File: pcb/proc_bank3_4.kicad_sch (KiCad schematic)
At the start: 2 parts, among them U1 XC6SLX9-TQG144

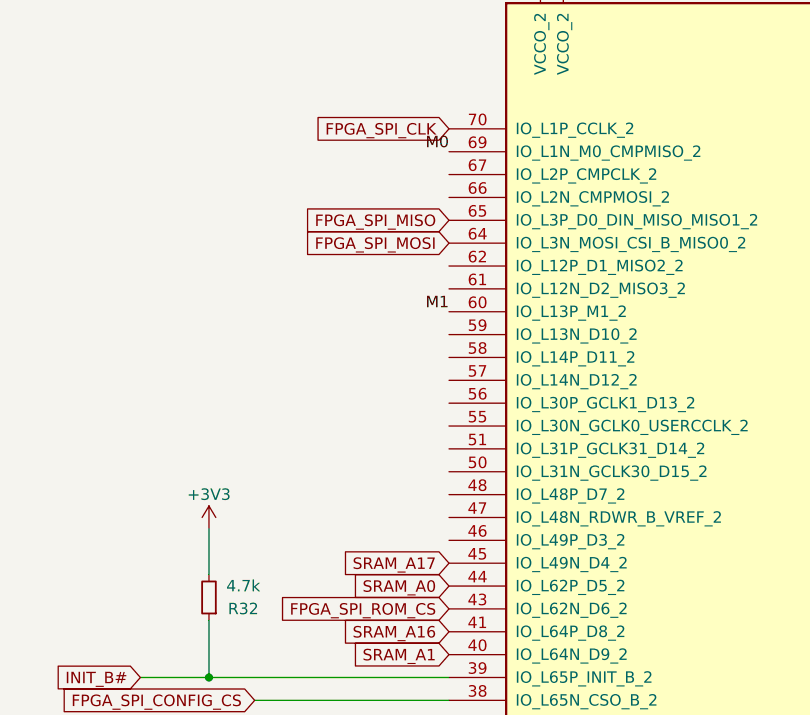
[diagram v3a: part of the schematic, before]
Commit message: edit the connector pinout
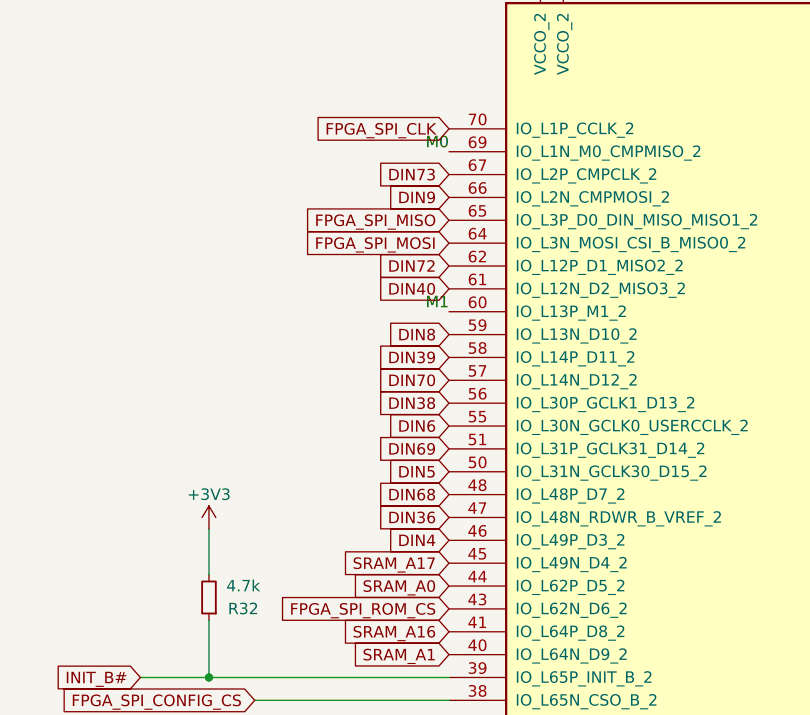
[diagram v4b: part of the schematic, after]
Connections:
- net DIN4: now reaches U1.46 (IO_L49P_D3_2)
- net DIN36: now reaches U1.47 (IO_L48N_RDWR_B_VREF_2)
- net DIN68: now reaches U1.48 (IO_L48P_D7_2)
- net DIN5: now reaches U1.50 (IO_L31N_GCLK30_D15_2)
- net DIN69: now reaches U1.51 (IO_L31P_GCLK31_D14_2)
- net DIN6: now reaches U1.55 (IO_L30N_GCLK0_USERCCLK_2)
- net DIN38: now reaches U1.56 (IO_L30P_GCLK1_D13_2)
- net DIN70: now reaches U1.57 (IO_L14N_D12_2)
- net DIN39: now reaches U1.58 (IO_L14P_D11_2)
- net DIN8: now reaches U1.59 (IO_L13N_D10_2)
- net DIN40: now reaches U1.61 (IO_L12N_D2_MISO3_2)
- net DIN72: now reaches U1.62 (IO_L12P_D1_MISO2_2)
- net DIN9: now reaches U1.66 (IO_L2N_CMPMOSI_2)
- net DIN73: now reaches U1.67 (IO_L2P_CMPCLK_2)
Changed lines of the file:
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@@
-(kicad_sch (version 20210621) (generator eeschema)
+(kicad_sch (version 20210406) (generator eeschema)
   (paper "User" 280.01 180.01)
   (junction (at 107.95 116.84) (diameter 0.9144) (color 0 0 0 0))
@@
     )
   )
+  (global_label "DIN73" (shape input) (at 134.62 60.96 180) (fields_autoplaced)
+    (effects (font (size 1.27 1.27)) (justify right))
+    (property "Intersheet References" "${INTERSHEET_REFS}" (id 0) (at 126.5826 60.8806 0)
+      (effects (font (size 1.27 1.27)) (justify right) hide)
+    )
+  )
+  (global_label "DIN9" (shape input) (at 134.62 63.5 180) (fields_autoplaced)
+    (effects (font (size 1.27 1.27)) (justify right))
+    (property "Intersheet References" "${INTERSHEET_REFS}" (id 0) (at 127.7921 63.4206 0)
+      (effects (font (size 1.27 1.27)) (justify right) hide)
+    )
+  )
   (global_label "FPGA_SPI_MISO" (shape input) (at 134.62 66.04 180) (fields_autoplaced)
     (effects (font (size 1.27 1.27)) (justify right))
@@
       (effects (font (size 1.27 1.27)) (justify right) hide)
     )
+  )
+  (global_label "DIN72" (shape input) (at 134.62 71.12 180) (fields_autoplaced)
+    (effects (font (size 1.27 1.27)) (justify right))
+    (property "Intersheet References" "${INTERSHEET_REFS}" (id 0) (at 126.5826 71.0406 0)
+      (effects (font (size 1.27 1.27)) (justify right) hide)
+    )
+  )
+  (global_label "DIN40" (shape input) (at 134.62 73.66 180) (fields_autoplaced)
+    (effects (font (size 1.27 1.27)) (justify right))
+    (property "Intersheet References" "${INTERSHEET_REFS}" (id 0) (at 126.5826 73.5806 0)
+      (effects (font (size 1.27 1.27)) (justify right) hide)
+    )
+  )
+  (global_label "DIN8" (shape input) (at 134.62 78.74 180) (fields_autoplaced)
+    (effects (font (size 1.27 1.27)) (justify right))
+    (property "Intersheet References" "${INTERSHEET_REFS}" (id 0) (at 127.7921 78.6606 0)
+      (effects (font (size 1.27 1.27)) (justify right) hide)
+    )
+  )
+  (global_label "DIN39" (shape input) (at 134.62 81.28 180) (fields_autoplaced)
+    (effects (font (size 1.27 1.27)) (justify right))
+    (property "Intersheet References" "${INTERSHEET_REFS}" (id 0) (at 126.5826 81.2006 0)
+      (effects (font (size 1.27 1.27)) (justify right) hide)
+    )
+  )
+  (global_label "DIN70" (shape input) (at 134.62 83.82 180) (fields_autoplaced)
+    (effects (font (size 1.27 1.27)) (justify right))
+    (property "Intersheet References" "${INTERSHEET_REFS}" (id 0) (at 126.5826 83.7406 0)
+      (effects (font (size 1.27 1.27)) (justify right) hide)
+    )
+  )
+  (global_label "DIN38" (shape input) (at 134.62 86.36 180) (fields_autoplaced)
+    (effects (font (size 1.27 1.27)) (justify right))
+    (property "Intersheet References" "${INTERSHEET_REFS}" (id 0) (at 126.5826 86.2806 0)
+      (effects (font (size 1.27 1.27)) (justify right) hide)
+    )
+  )
+  (global_label "DIN6" (shape input) (at 134.62 88.9 180) (fields_autoplaced)
+    (effects (font (size 1.27 1.27)) (justify right))
+    (property "Intersheet References" "${INTERSHEET_REFS}" (id 0) (at 127.7921 88.8206 0)
+      (effects (font (size 1.27 1.27)) (justify right) hide)
+    )
+  )
+  (global_label "DIN69" (shape input) (at 134.62 91.44 180) (fields_autoplaced)
+    (effects (font (size 1.27 1.27)) (justify right))
+    (property "Intersheet References" "${INTERSHEET_REFS}" (id 0) (at 126.5826 91.3606 0)
+      (effects (font (size 1.27 1.27)) (justify right) hide)
+    )
+  )
+  (global_label "DIN5" (shape input) (at 134.62 93.98 180) (fields_autoplaced)
+    (effects (font (size 1.27 1.27)) (justify right))
+    (property "Intersheet References" "${INTERSHEET_REFS}" (id 0) (at 127.7921 93.9006 0)
+      (effects (font (size 1.27 1.27)) (justify right) hide)
+    )
+  )
+  (global_label "DIN68" (shape input) (at 134.62 96.52 180) (fields_autoplaced)
+    (effects (font (size 1.27 1.27)) (justify right))
+    (property "Intersheet References" "${INTERSHEET_REFS}" (id 0) (at 126.5826 96.4406 0)
+      (effects (font (size 1.27 1.27)) (justify right) hide)
+    )
+  )
+  (global_label "DIN36" (shape input) (at 134.62 99.06 180) (fields_autoplaced)
+    (effects (font (size 1.27 1.27)) (justify right))
+    (property "Intersheet References" "${INTERSHEET_REFS}" (id 0) (at 126.5826 98.9806 0)
+      (effects (font (size 1.27 1.27)) (justify right) hide)
+    )
+  )
+  (global_label "DIN4" (shape input) (at 134.62 101.6 180) (fields_autoplaced)
+    (effects (font (size 1.27 1.27)) (justify right))
+    (property "Intersheet References" "${INTERSHEET_REFS}" (id 0) (at 127.7921 101.5206 0)
+      (effects (font (size 1.27 1.27)) (justify right) hide)
+    )
